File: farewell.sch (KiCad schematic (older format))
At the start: 42 parts, among them SW1 SW_Push, U1 0

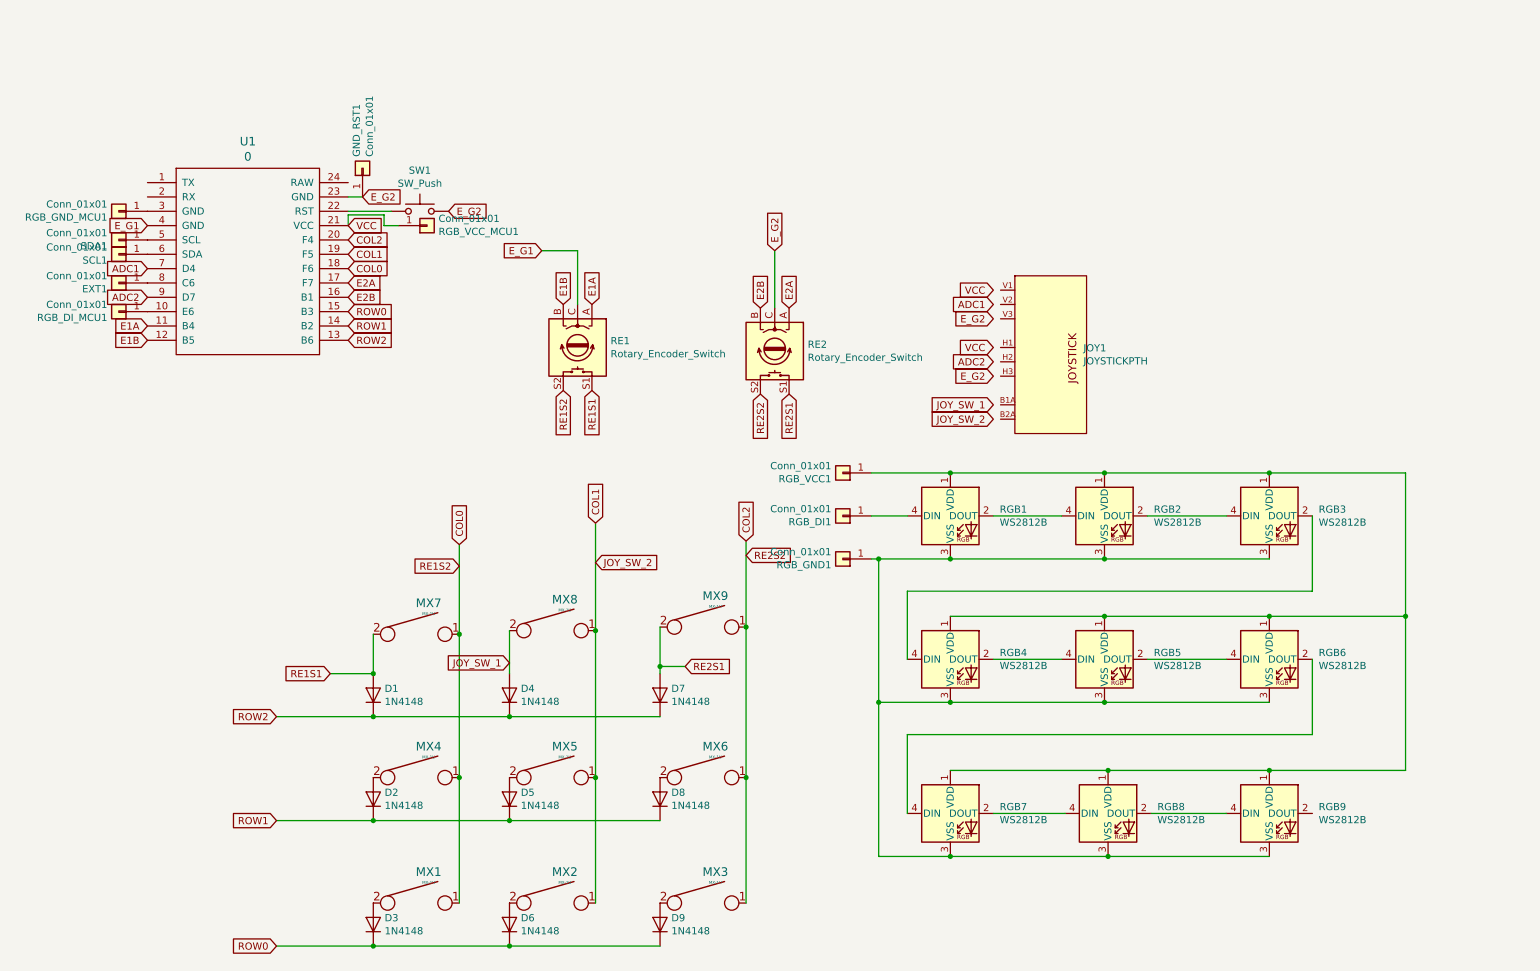
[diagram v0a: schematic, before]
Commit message: rgb support with castellated connection
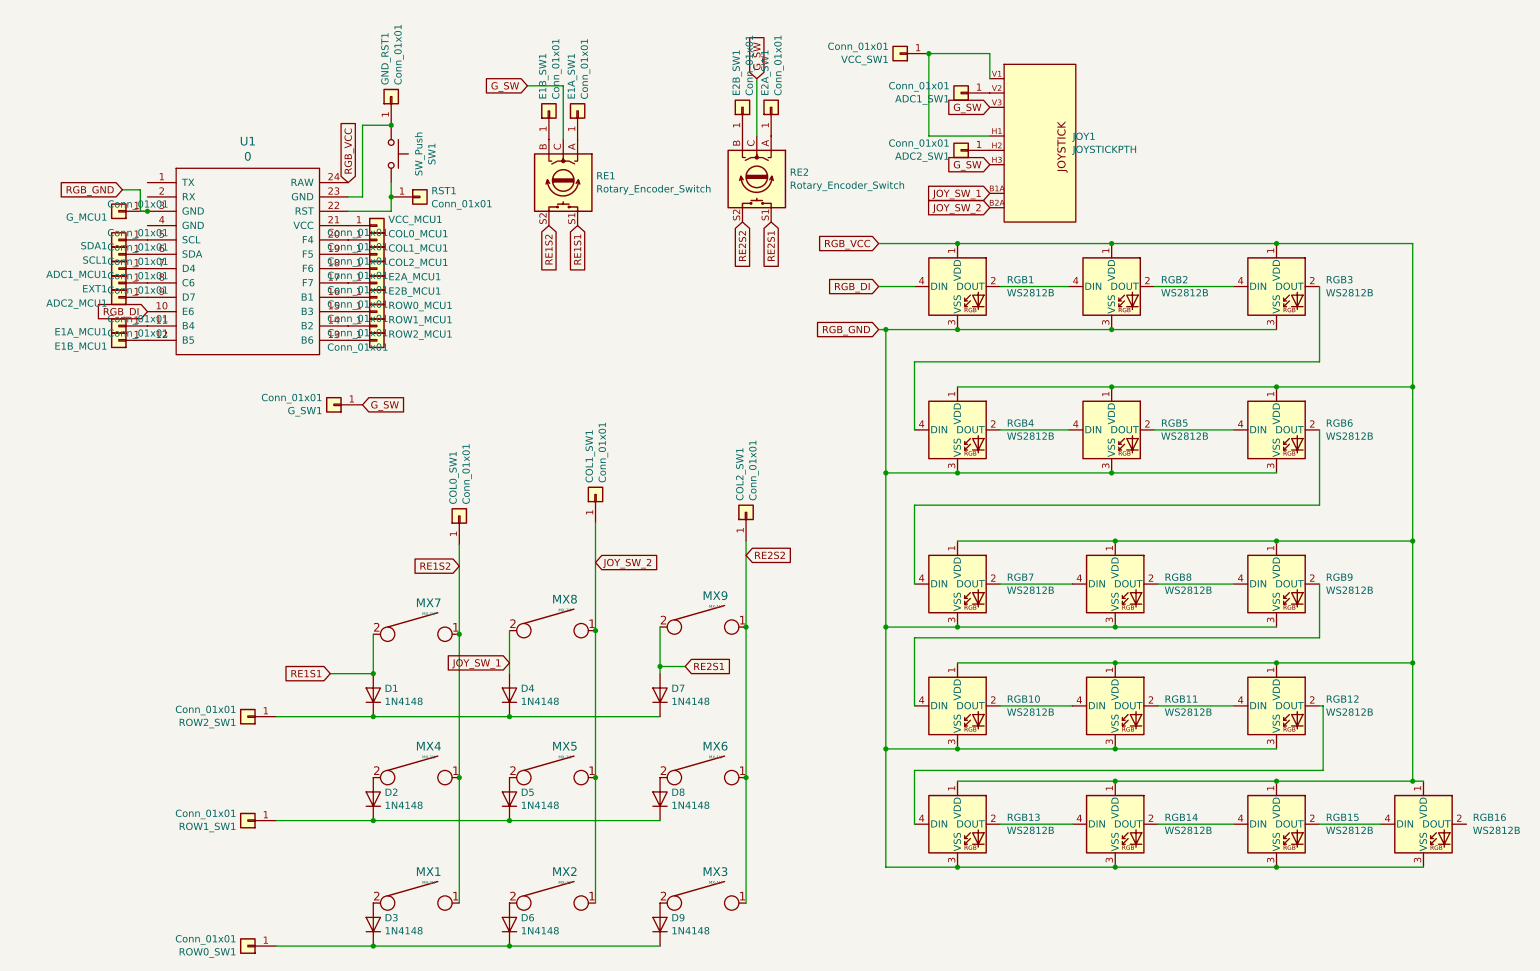
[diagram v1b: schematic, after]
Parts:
- removed RGB_DI1, RGB_DI_MCU1, RGB_GND1, RGB_GND_MCU1, RGB_VCC1, RGB_VCC_MCU1: Conn_01x01, keyboard_parts:PIN_1, symbol Connector_Generic:Conn_01x01
- added ADC1_MCU1, ADC1_SW1, ADC2_MCU1, ADC2_SW1, COL0_MCU1, COL0_SW1, COL1_MCU1, COL1_SW1, COL2_MCU1, COL2_SW1, E1A_MCU1, E1A_SW1, E1B_MCU1, E1B_SW1, E2A_MCU1, E2A_SW1, E2B_MCU1, E2B_SW1, G_MCU1, G_SW1, ROW0_MCU1, ROW0_SW1, ROW1_MCU1, ROW1_SW1, ROW2_MCU1, ROW2_SW1, RST1, VCC_MCU1, VCC_SW1: Conn_01x01, keyboard_parts:PIN_1, symbol Connector_Generic:Conn_01x01
- added RGB10, RGB11, RGB12, RGB13, RGB14, RGB15, RGB16: WS2812B, LED_SMD:LED_WS2812B_PLCC4_5.0x5.0mm_P3.2mm, symbol LED:WS2812B
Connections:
- net JOY_SW_1: now also JOY1.B1A (SEL+)
- net JOY_SW_2: now reaches JOY1.B2A (SEL-)
- net JOY_SW_2: now also MX2.1, MX5.1, MX8.1, COL1_SW1.1 (Pin_1)
- net at JOY1.H1 (H+): now also JOY1.V1 (V+), VCC_SW1.1 (Pin_1)
- net at JOY1.H2 (H): now also ADC2_SW1.1 (Pin_1)
- net G_SW: now reaches JOY1.H3 (H-)
- net G_SW: now also JOY1.V3 (V-), RE1.C, RE2.C, G_SW1.1 (Pin_1)
- net at JOY1.V2 (V): now also ADC1_SW1.1 (Pin_1)
- net at SW1.1: now also GND_RST1.1 (Pin_1), U1.23 (GND); no longer U1.22 (RST)
- net RGB_DI: now reaches U1.10 (E6)
- net RGB_DI: now also RGB1.4 (DIN)
- net RGB_VCC: now reaches U1.24 (RAW)
- net RGB_VCC: now also RGB1.1 (VDD), RGB2.1 (VDD), RGB3.1 (VDD), RGB4.1 (VDD), RGB5.1 (VDD), RGB6.1 (VDD), RGB7.1 (VDD), RGB8.1 (VDD), RGB9.1 (VDD), RGB10.1 (VDD), RGB11.1 (VDD), RGB12.1 (VDD), RGB13.1 (VDD), RGB14.1 (VDD), RGB15.1 (VDD), RGB16.1 (VDD)
- net RGB_GND: now reaches U1.3 (GND)
- net RGB_GND: now also RGB1.3 (VSS), RGB2.3 (VSS), RGB3.3 (VSS), RGB4.3 (VSS), RGB5.3 (VSS), RGB6.3 (VSS), RGB7.3 (VSS), RGB8.3 (VSS), RGB9.3 (VSS), G_MCU1.1 (Pin_1), RGB10.3 (VSS), RGB11.3 (VSS), RGB12.3 (VSS), RGB13.3 (VSS), RGB14.3 (VSS), RGB15.3 (VSS), RGB16.3 (VSS)
- net at RGB9.2 (DOUT): now also RGB10.4 (DIN)
- net ADC1: no longer names the net of U1.7 (D4)
- net ADC1: now also ADC1_MCU1.1 (Pin_1)
- net ADC2: no longer names the net of U1.9 (D7)
- net ADC2: now also ADC2_MCU1.1 (Pin_1)
- net COL0 renamed RE1S2
- net RE1S2: now also COL0_SW1.1 (Pin_1); no longer U1.18 (F6)
- removed net COL1: MX2.1, MX5.1, MX8.1, U1.19 (F5)
- net COL2 renamed RE2S2
- net RE2S2: now also COL2_SW1.1 (Pin_1); no longer U1.20 (F4)
- net E1A: no longer names the net of RE1.A
- net E1A: now also E1A_SW1.1 (Pin_1); no longer U1.11 (B4)
- net E1B: no longer names the net of RE1.B
- net E1B: now also E1B_SW1.1 (Pin_1); no longer U1.12 (B5)
- net E2A: no longer names the net of RE2.A
- net E2A: now also E2A_SW1.1 (Pin_1); no longer U1.17 (F7)
- net E2B: no longer names the net of RE2.B
- net E2B: now also E2B_SW1.1 (Pin_1); no longer U1.16 (B1)
- net E_G1: no longer names the net of U1.4 (GND)
- net E_G1: no longer RE1.C
- removed net E_G2: GND_RST1.1 (Pin_1), RE2.C, SW1.2, U1.23 (GND)
- net ROW0: no longer names the net of D3.1 (K), D6.1 (K), D9.1 (K)
- net ROW0: now also ROW0_SW1.1 (Pin_1); no longer U1.15 (B3)
- net ROW1: no longer names the net of D2.1 (K), D5.1 (K), D8.1 (K)
- net ROW1: now also ROW1_SW1.1 (Pin_1); no longer U1.14 (B2)
- net ROW2: no longer names the net of D1.1 (K), D4.1 (K), D7.1 (K)
- net ROW2: now also ROW2_SW1.1 (Pin_1); no longer U1.13 (B6)
- net VCC: no longer names the net of U1.21 (VCC)
- net VCC: now also VCC_MCU1.1 (Pin_1)
- new net: RST1.1 (Pin_1), SW1.2, U1.22 (RST)
- new net: E1A_MCU1.1 (Pin_1), U1.11 (B4)
- new net: E1B_MCU1.1 (Pin_1), U1.12 (B5)
- new net: ROW2_MCU1.1 (Pin_1), U1.13 (B6)
- new net: ROW1_MCU1.1 (Pin_1), U1.14 (B2)
- new net: ROW0_MCU1.1 (Pin_1), U1.15 (B3)
- new net: E2B_MCU1.1 (Pin_1), U1.16 (B1)
- new net: E2A_MCU1.1 (Pin_1), U1.17 (F7)
- new net: COL2_MCU1.1 (Pin_1), U1.18 (F6)
- new net: COL1_MCU1.1 (Pin_1), U1.19 (F5)
- new net: COL0_MCU1.1 (Pin_1), U1.20 (F4)
- new net: RGB12.2 (DOUT), RGB13.4 (DIN)
- new net: RGB11.2 (DOUT), RGB12.4 (DIN)
- new net: RGB10.2 (DOUT), RGB11.4 (DIN)
- new net: RGB13.2 (DOUT), RGB14.4 (DIN)
- new net: RGB14.2 (DOUT), RGB15.4 (DIN)
- new net: RGB15.2 (DOUT), RGB16.4 (DIN)
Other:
- moved on the sheet: GND_RST1, JOY1, RE1, RE2, RGB1, RGB2, RGB3, RGB4, RGB5, RGB6, RGB7, RGB8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

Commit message: use female header pins for connecting switch pcb to mcu pcb
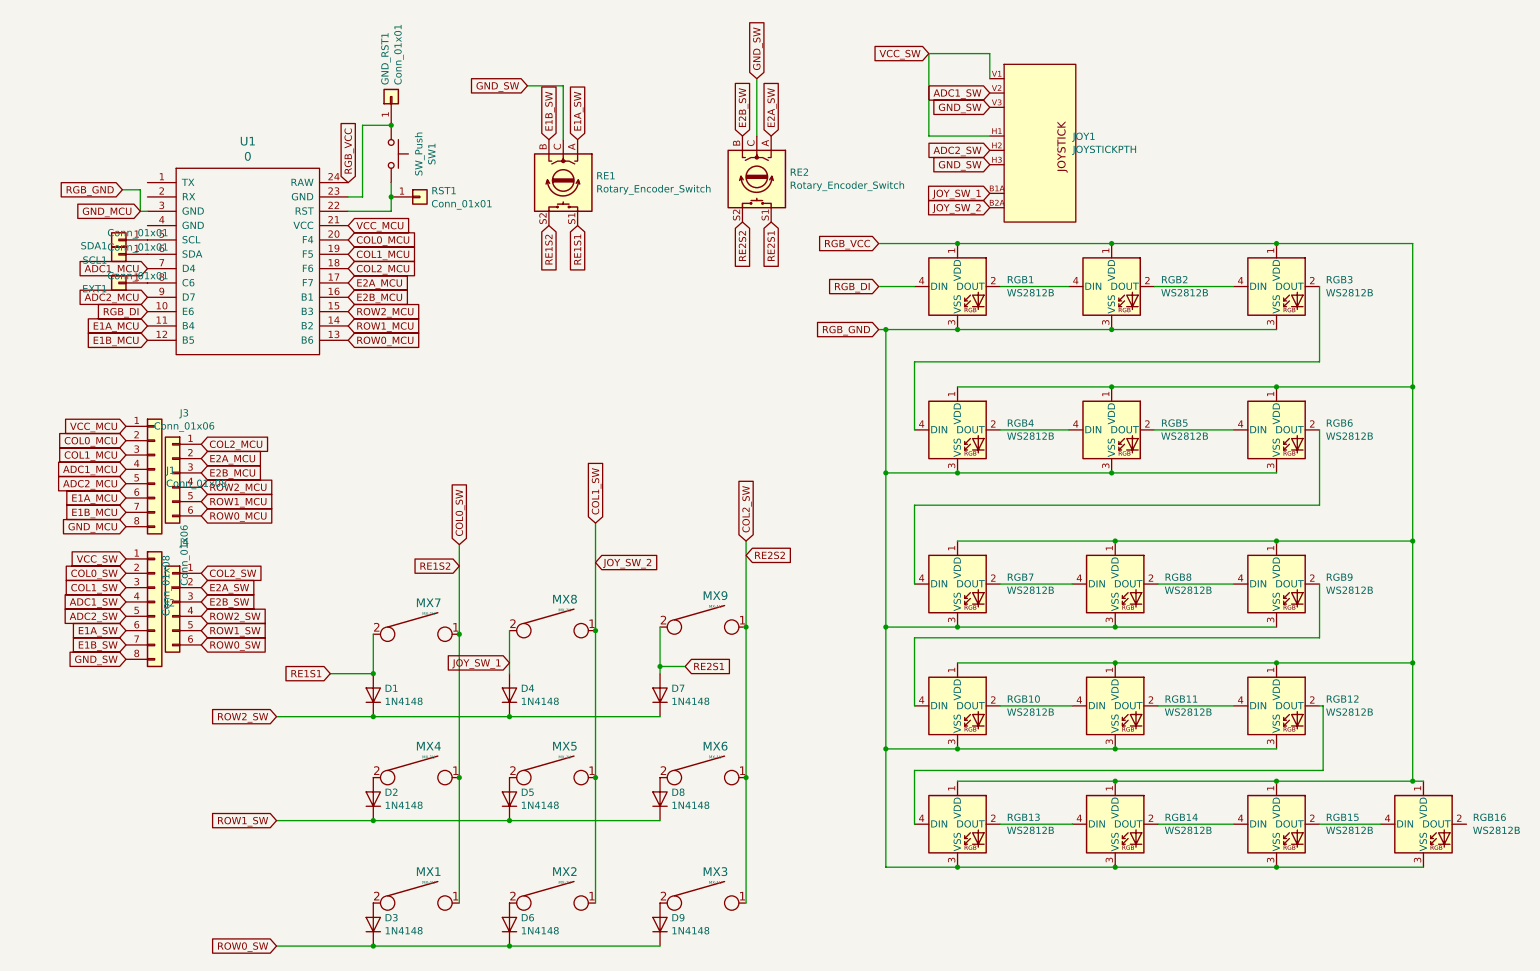
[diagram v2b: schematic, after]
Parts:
- removed ADC1_MCU1, ADC1_SW1, ADC2_MCU1, ADC2_SW1, COL0_MCU1, COL0_SW1, COL1_MCU1, COL1_SW1, COL2_MCU1, COL2_SW1, E1A_MCU1, E1A_SW1, E1B_MCU1, E1B_SW1, E2A_MCU1, E2A_SW1, E2B_MCU1, E2B_SW1, G_MCU1, G_SW1, ROW0_MCU1, ROW0_SW1, ROW1_MCU1, ROW1_SW1, ROW2_MCU1, ROW2_SW1, VCC_MCU1, VCC_SW1: Conn_01x01, keyboard_parts:PIN_1, symbol Connector_Generic:Conn_01x01
- added J1, J2: Conn_01x08, farewell_pcb:keebio_Header-8-Pin-ZigZag, symbol Connector_Generic:Conn_01x08
- added J3, J4: Conn_01x06, farewell_pcb:keebio_Header-6-Pin-ZigZag, symbol Connector_Generic:Conn_01x06
- U1: footprint promicro:ProMicro -> farewell_pcb:keebio_ArduinoProMicro-ZigZag
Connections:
- net E1A_SW: now reaches RE1.A
- net E1A_SW: now also J2.6 (Pin_6)
- net E1B_SW: now reaches RE1.B
- net E1B_SW: now also J2.7 (Pin_7)
- net E2A_SW: now reaches RE2.A
- net E2A_SW: now also J4.2 (Pin_2)
- net E2B_SW: now reaches RE2.B
- net E2B_SW: now also J4.3 (Pin_3)
- net ROW0_SW: now reaches D3.1 (K), D6.1 (K), D9.1 (K)
- net ROW0_SW: now also J4.6 (Pin_6)
- net ROW1_SW: now reaches D2.1 (K), D5.1 (K), D8.1 (K)
- net ROW1_SW: now also J4.5 (Pin_5)
- net ROW2_SW: now reaches D1.1 (K), D4.1 (K), D7.1 (K)
- net ROW2_SW: now also J4.4 (Pin_4)
- net VCC_SW: now reaches JOY1.H1 (H+), JOY1.V1 (V+)
- net VCC_SW: now also J2.1 (Pin_1)
- net ADC2_SW: now reaches JOY1.H2 (H)
- net ADC2_SW: now also J2.5 (Pin_5)
- net ADC1_SW: now reaches JOY1.V2 (V)
- net ADC1_SW: now also J2.4 (Pin_4)
- net E1A_MCU: now reaches U1.11 (B4)
- net E1A_MCU: now also J1.6 (Pin_6)
- net E1B_MCU: now reaches U1.12 (B5)
- net E1B_MCU: now also J1.7 (Pin_7)
- net ROW0_MCU: now reaches U1.13 (B6)
- net ROW0_MCU: now also J3.6 (Pin_6)
- net ROW1_MCU: now reaches U1.14 (B2)
- net ROW1_MCU: now also J3.5 (Pin_5)
- net ROW2_MCU: now reaches U1.15 (B3)
- net ROW2_MCU: now also J3.4 (Pin_4)
- net E2B_MCU: now reaches U1.16 (B1)
- net E2B_MCU: now also J3.3 (Pin_3)
- net E2A_MCU: now reaches U1.17 (F7)
- net E2A_MCU: now also J3.2 (Pin_2)
- net COL2_MCU: now reaches U1.18 (F6)
- net COL2_MCU: now also J3.1 (Pin_1)
- net COL1_MCU: now reaches U1.19 (F5)
- net COL1_MCU: now also J1.3 (Pin_3)
- net COL0_MCU: now reaches U1.20 (F4)
- net COL0_MCU: now also J1.2 (Pin_2)
- net VCC_MCU: now reaches U1.21 (VCC)
- net VCC_MCU: now also J1.1 (Pin_1)
- net ADC1_MCU: now reaches U1.7 (D4)
- net ADC1_MCU: now also J1.4 (Pin_4)
- net ADC2_MCU: now reaches U1.9 (D7)
- net ADC2_MCU: now also J1.5 (Pin_5)
- net G_SW renamed GND_SW
- net GND_SW: now also J2.8 (Pin_8)
- net JOY_SW_2 renamed COL1_SW
- net COL1_SW: now also J2.3 (Pin_3)
- net RE1S2 renamed COL0_SW
- net COL0_SW: now also J2.2 (Pin_2)
- net RE2S2 renamed COL2_SW
- net COL2_SW: now also J4.1 (Pin_1)
- net RGB_GND renamed GND_MCU
- net GND_MCU: now also J1.8 (Pin_8)

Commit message: pcb with hybrid sk6812 mini-e/ws2812B footprint and mx/choc compatible switch footprint
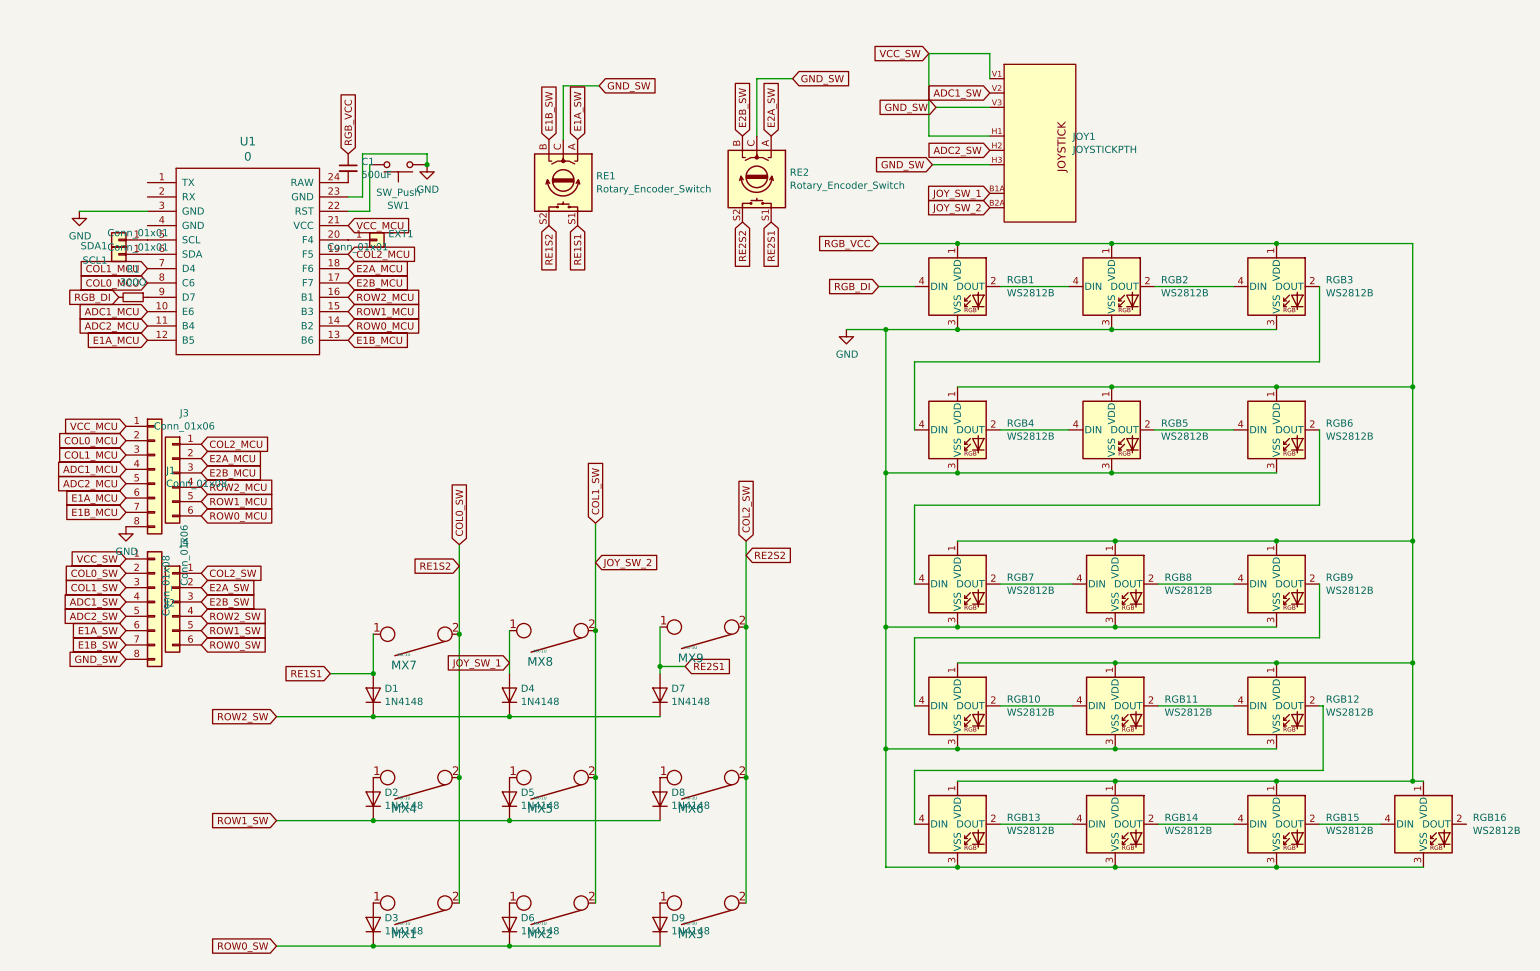
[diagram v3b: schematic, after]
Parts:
- removed GND_RST1, RST1: Conn_01x01, keyboard_parts:PIN_1, symbol Connector_Generic:Conn_01x01
- added C1: 500uF, Capacitor_THT:CP_Radial_D8.0mm_P3.50mm, symbol Device:C_Small
- added R1: 300O, Resistor_THT:R_Axial_DIN0207_L6.3mm_D2.5mm_P7.62mm_Horizontal, symbol Device:R_Small
- MX1, MX2, MX3, MX4, MX5, MX6, MX7, MX8, MX9: footprint farewell:MX-1U-NoLED-NoPCBMount -> keebio:MX-Alps-Choc-1U-NoLED
- RGB1, RGB10, RGB11, RGB12, RGB13, RGB14, RGB15, RGB16, RGB2, RGB3, RGB4, RGB5, RGB6, RGB7, RGB8, RGB9: footprint LED_SMD:LED_WS2812B_PLCC4_5.0x5.0mm_P3.2mm -> farewell_pcb:LED_WS2812B_SK6812_MINI-E_HYBRID
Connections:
- net GND_MCU is gone; now on net GND: J1.8 (Pin_8), RGB1.3 (VSS), RGB10.3 (VSS), RGB11.3 (VSS), RGB12.3 (VSS), RGB13.3 (VSS), RGB14.3 (VSS), RGB15.3 (VSS), RGB16.3 (VSS), RGB2.3 (VSS), RGB3.3 (VSS), RGB4.3 (VSS), RGB5.3 (VSS), RGB6.3 (VSS), RGB7.3 (VSS), RGB8.3 (VSS), RGB9.3 (VSS), U1.3 (GND)
- net ADC1_MCU: now also U1.10 (E6); no longer U1.7 (D4)
- net ADC2_MCU: now also U1.11 (B4); no longer U1.9 (D7)
- net COL0_MCU: now also U1.8 (C6); no longer U1.20 (F4)
- net COL0_SW: now also MX1.2, MX4.2, MX7.2; no longer MX1.1, MX4.1, MX7.1
- net COL1_MCU: now also U1.7 (D4); no longer U1.19 (F5)
- net COL1_SW: now also MX2.2, MX5.2, MX8.2; no longer MX2.1, MX5.1, MX8.1
- net COL2_MCU: now also U1.19 (F5); no longer U1.18 (F6)
- net COL2_SW: now also MX3.2, MX6.2, MX9.2; no longer MX3.1, MX6.1, MX9.1
- net E1A_MCU: now also U1.12 (B5); no longer U1.11 (B4)
- net E1B_MCU: now also U1.13 (B6); no longer U1.12 (B5)
- net E2A_MCU: now also U1.18 (F6); no longer U1.17 (F7)
- net E2B_MCU: now also U1.17 (F7); no longer U1.16 (B1)
- net JOY_SW_1: now also MX8.1; no longer MX8.2
- net RE1S1: now also MX7.1; no longer MX7.2
- net RE2S1: now also MX9.1; no longer MX9.2
- net RGB_DI: now also R1.2; no longer U1.10 (E6)
- net RGB_VCC: now also C1.1; no longer U1.24 (RAW)
- net ROW0_MCU: now also U1.14 (B2); no longer U1.13 (B6)
- net ROW1_MCU: now also U1.15 (B3); no longer U1.14 (B2)
- net ROW2_MCU: now also U1.16 (B1); no longer U1.15 (B3)
- net at D3.2 (A): now also MX1.1; no longer MX1.2
- net at D6.2 (A): now also MX2.1; no longer MX2.2
- net at D9.2 (A): now also MX3.1; no longer MX3.2
- net at D2.2 (A): now also MX4.1; no longer MX4.2
- net at D5.2 (A): now also MX5.1; no longer MX5.2
- net at D8.2 (A): now also MX6.1; no longer MX6.2
- net GND: now reaches SW1.1, U1.23 (GND)
- net at EXT1.1 (Pin_1): now also U1.20 (F4); no longer U1.8 (C6)
- new net: C1.2, U1.24 (RAW)
- new net: R1.1, U1.9 (D7)
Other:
- moved on the sheet: EXT1, MX1, MX2, MX3, MX4, MX5, MX6, MX7, MX8, MX9, SW1
